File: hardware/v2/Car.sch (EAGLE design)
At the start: 63 parts

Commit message: Completed Rev.A of v2 hardware.
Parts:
- removed POW: (no value), SparkFun-Connectors:M02PTH4
- added J1: (no value), con-jack:DCJ0303
- renumbered 3.3V to 3V3, ARMS1 to M.ARMS, DIO1 to AIO, LED1 to HB, LED2 to PWR
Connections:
- net +12V: now also J1.2; no longer POW.1
- net GND: now also J1.1; no longer POW.2

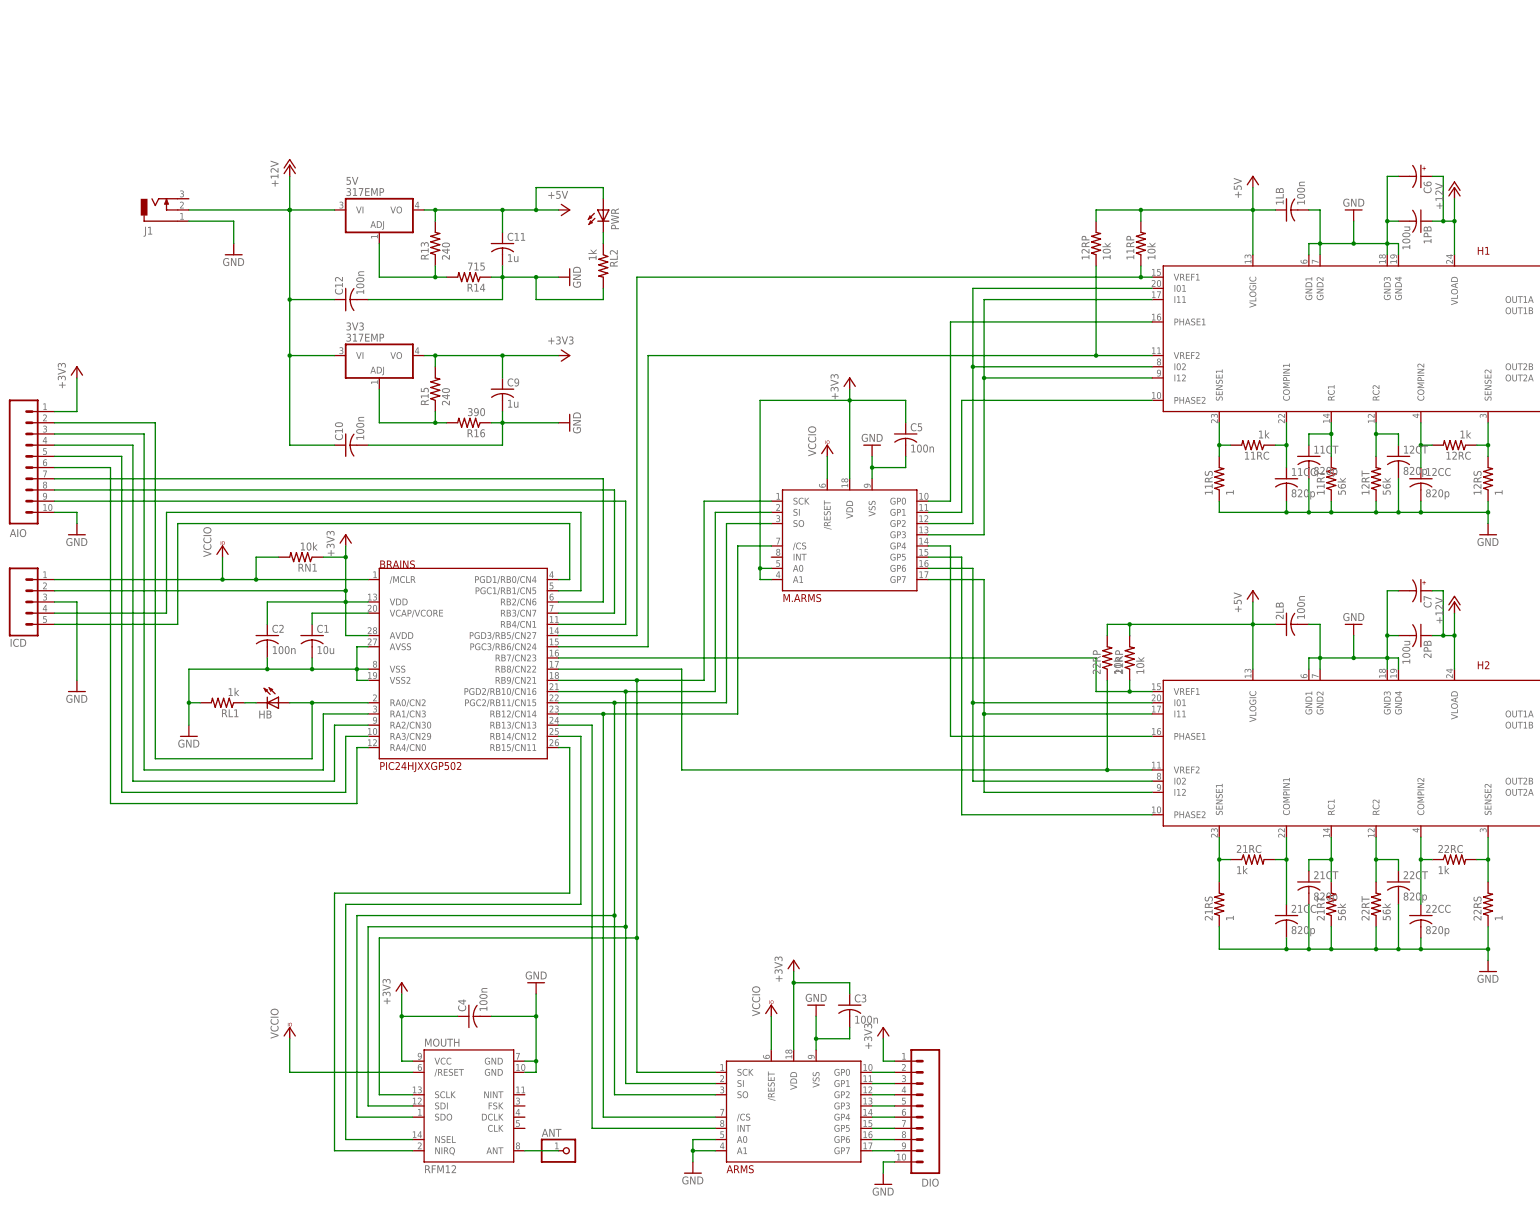
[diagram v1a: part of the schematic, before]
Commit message: Checkpointing. (about to make so potentially dangerous changes.)
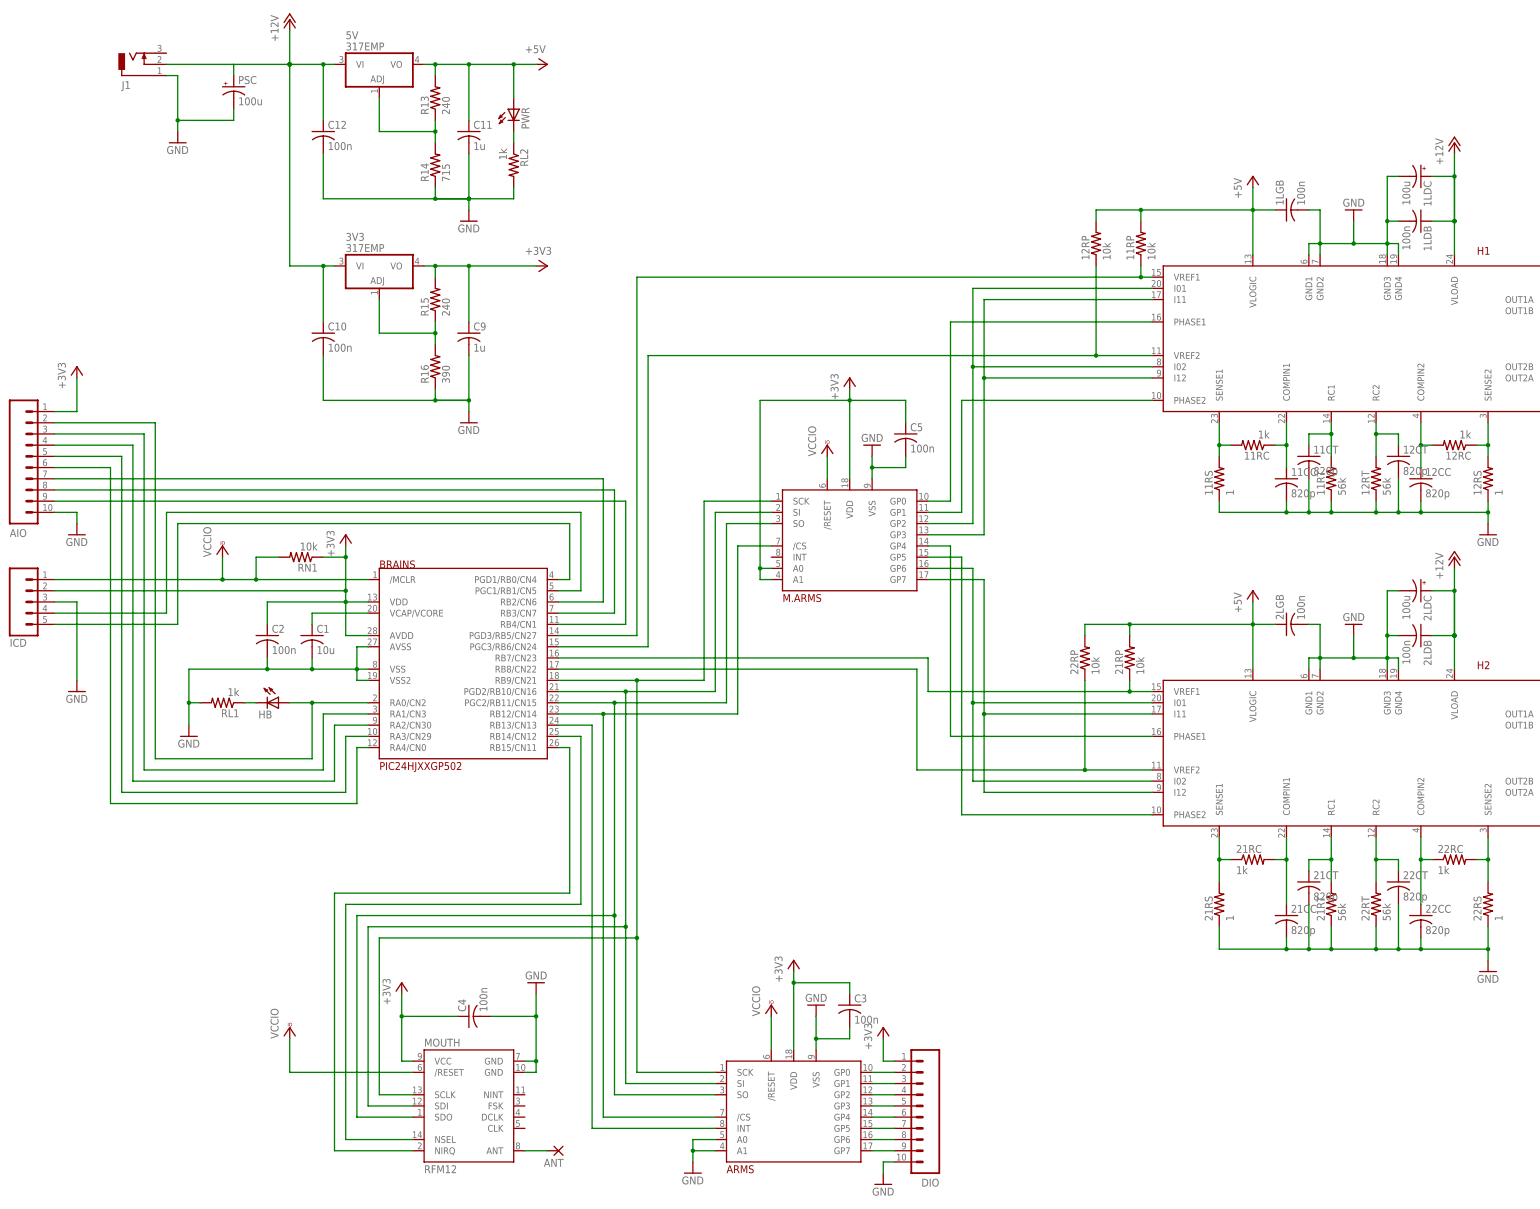
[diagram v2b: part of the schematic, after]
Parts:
- added PSC: 100u, SparkFun-Passives:CAP_POLC
- 1LDB, 2LDB: value 100u -> 100n
- 1LDC, 2LDC: value (none) -> 100u
- ANT: device pinhead:PINHD-1X1 -> wirepad:2,15/1,0
- renumbered 1LB to 1LGB, 1PB to 1LDB, 2LB to 2LGB, 2PB to 2LDB, C6 to 1LDC, C7 to 2LDC
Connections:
- removed net N$39: ANT.1, MOUTH.ANT
- new net N$11: ANT.P, MOUTH.ANT
- net +12V: now also PSC.+
- net GND: now also PSC.-
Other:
- moved on the sheet: 22RP, 3V3, 5V, C10, C11, C12, C9, J1, PWR, R13, R14, R15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

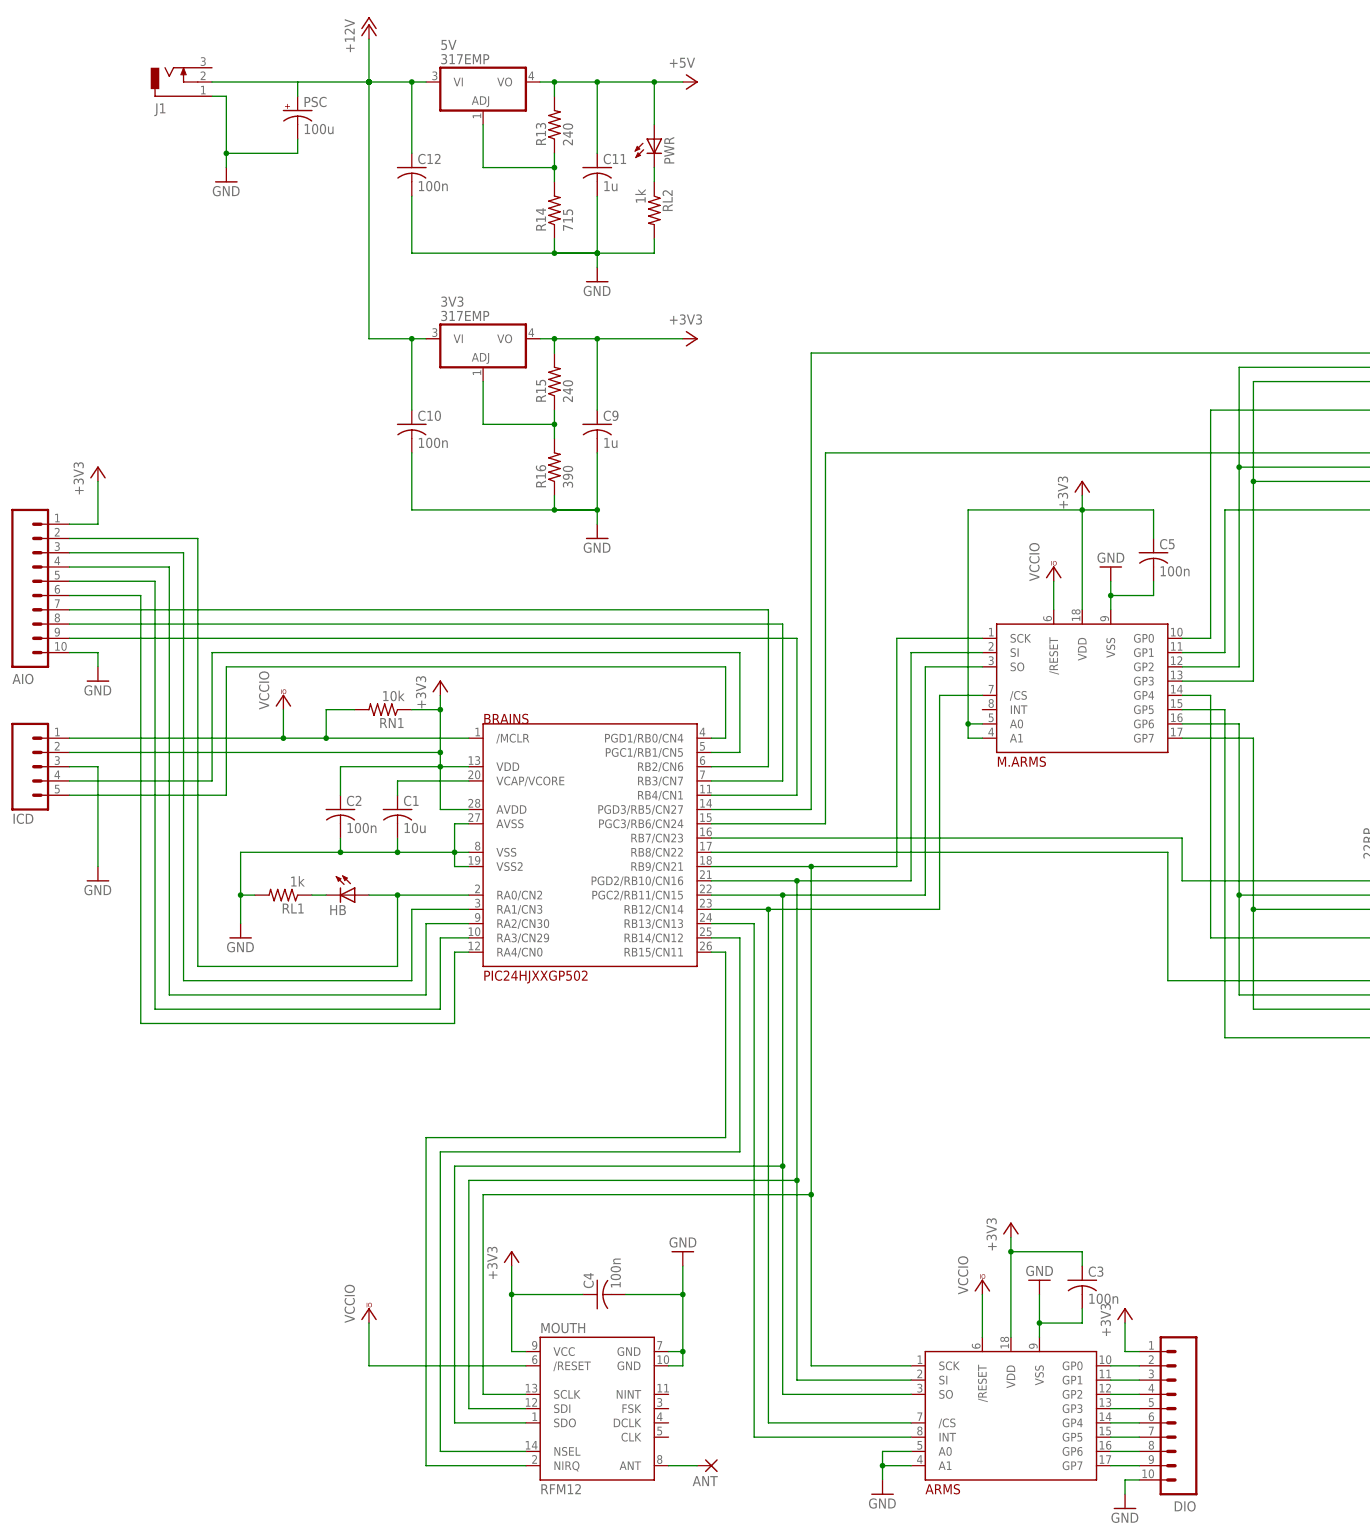
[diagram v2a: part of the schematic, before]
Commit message: Fixed a number of issues discovered from Rev. A boards.
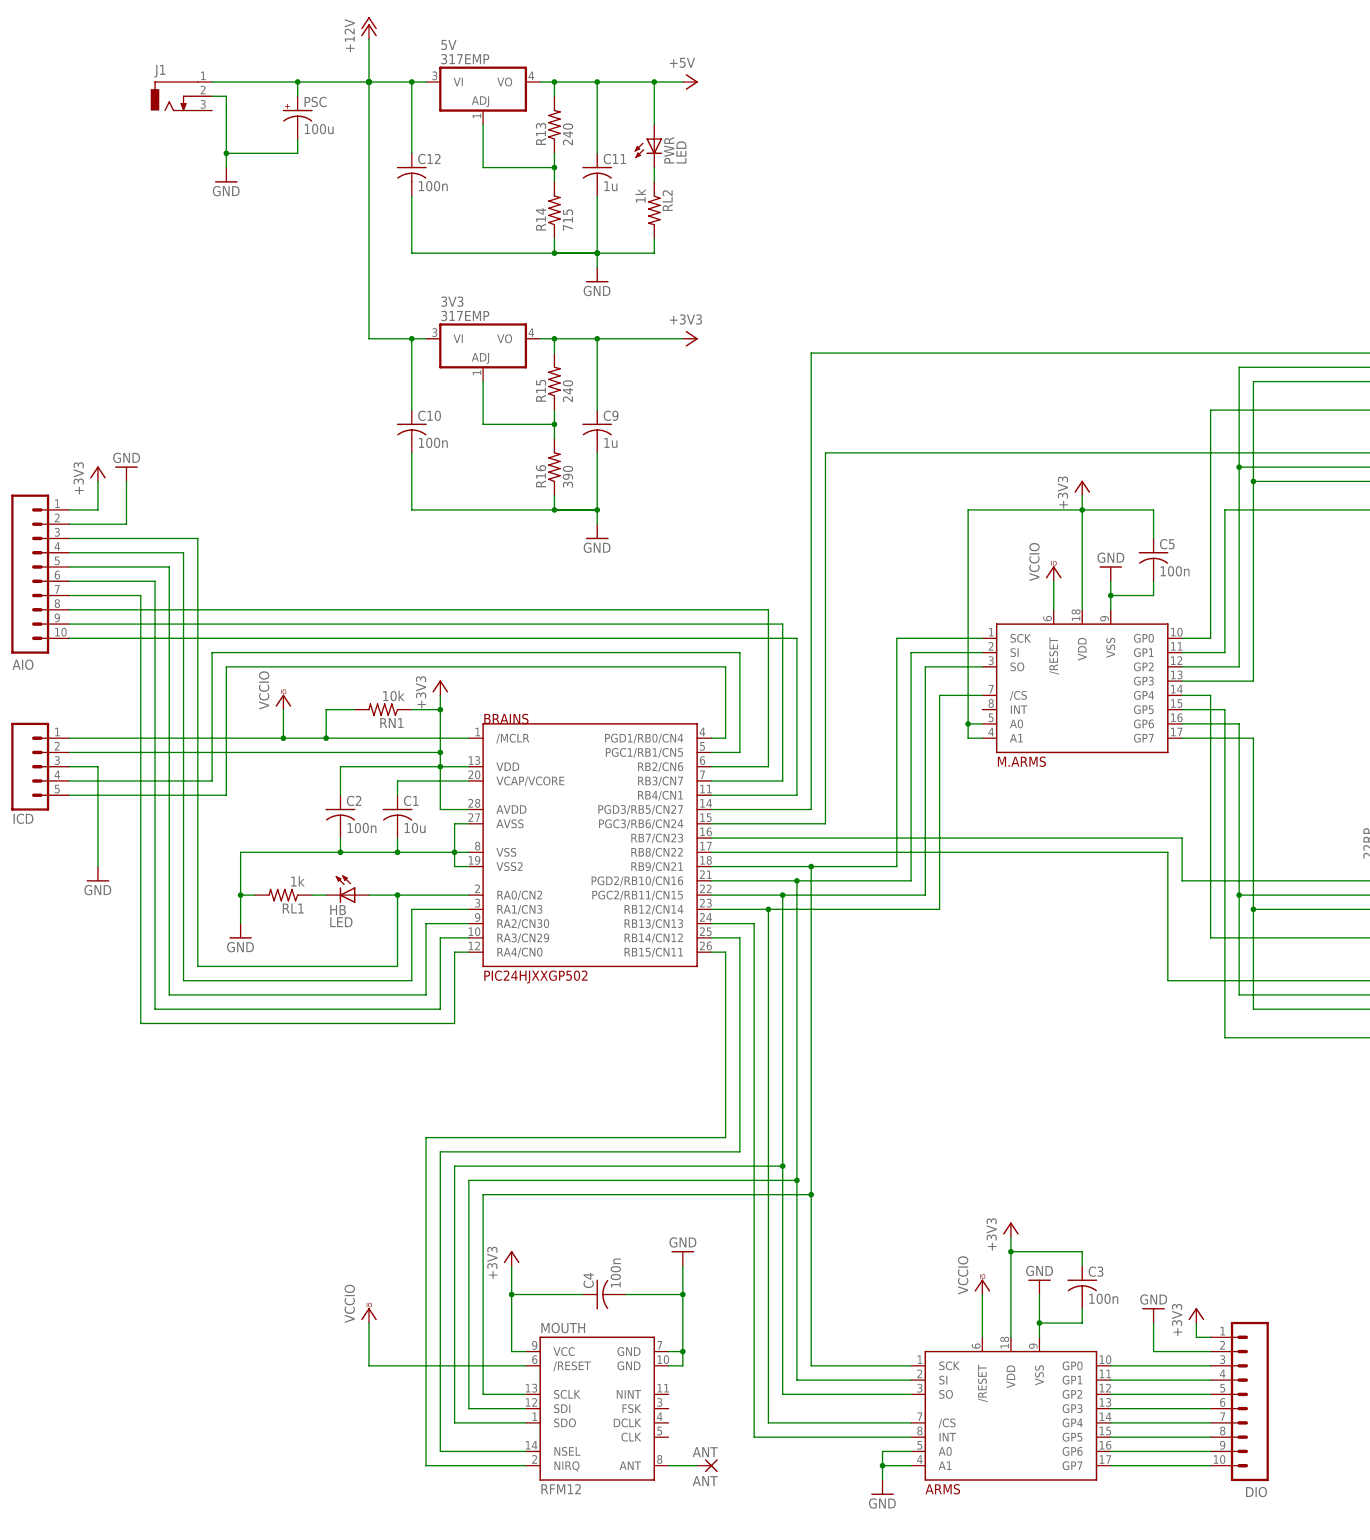
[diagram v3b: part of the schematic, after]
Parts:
- ANT: value (none) -> ANT
- HB, PWR: value (none) -> LED
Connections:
- removed net N$51: ARMS.GP5, DIO.7
- removed net N$52: ARMS.GP7, DIO.9
- new net N$39: ARMS.GP1, DIO.4
- new net N$47: ARMS.GP4, DIO.7
- net +12V: now also J1.1; no longer J1.2
- net GND: now also AIO.2, DIO.2, J1.2; no longer AIO.10, DIO.10, J1.1
- net N$12: now also ARMS.GP0, DIO.3; no longer ARMS.GP6, DIO.8
- net N$29: now also AIO.5; no longer AIO.4
- net N$32: now also AIO.6; no longer AIO.5
- net N$43: now also ARMS.GP2, DIO.5; no longer ARMS.GP0, DIO.2
- net N$44: now also ARMS.GP3, DIO.6; no longer ARMS.GP1, DIO.3
- net N$45: now also AIO.3; no longer AIO.2
- net N$48: now also ARMS.GP5, DIO.8; no longer ARMS.GP2, DIO.4
- net N$49: now also ARMS.GP6, DIO.9; no longer ARMS.GP3, DIO.5
- net N$50: now also ARMS.GP7, DIO.10; no longer ARMS.GP4, DIO.6
- net N$53: now also AIO.4; no longer AIO.3
- net N$54: now also AIO.8; no longer AIO.7
- net N$55: now also AIO.9; no longer AIO.8
- net N$57: now also AIO.7; no longer AIO.6
- net N$59: now also AIO.10; no longer AIO.9
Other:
- moved on the sheet: AIO, DIO, J1

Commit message: Minor cleanup.
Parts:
- removed C10, C12: 100n, rcl:C-USC0805
- removed PSC: 100u, SparkFun-Passives:CAP_POLC
- added PSB1: 100u, SparkFun-Passives:CAP_POLC
- added PSB2: 1u, rcl:C-USC0805
- added PSB3: 100n, rcl:C-USC0805
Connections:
- net +12V: now also PSB1.+, PSB2.1, PSB3.1; no longer C10.1, C12.1, PSC.+
- net GND: now also J1.3, PSB1.-, PSB2.2, PSB3.2; no longer C10.2, C12.2, J1.2, PSC.-
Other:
- moved on the sheet: J1

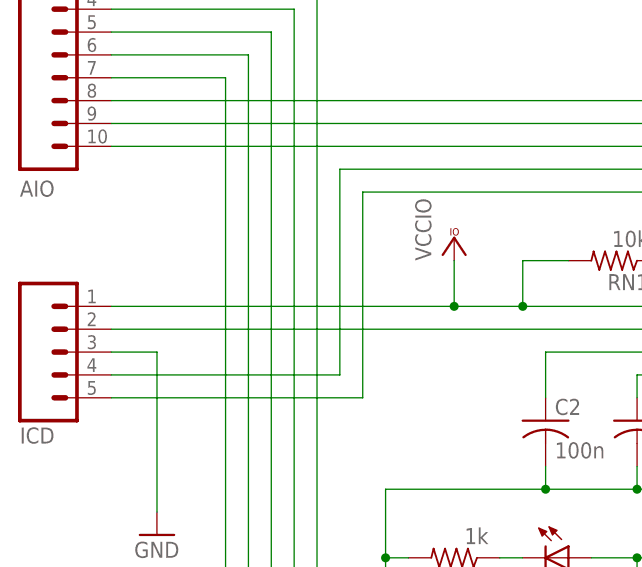
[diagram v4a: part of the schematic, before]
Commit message: Fixed PGD/PGC error (swapped) in schematic.
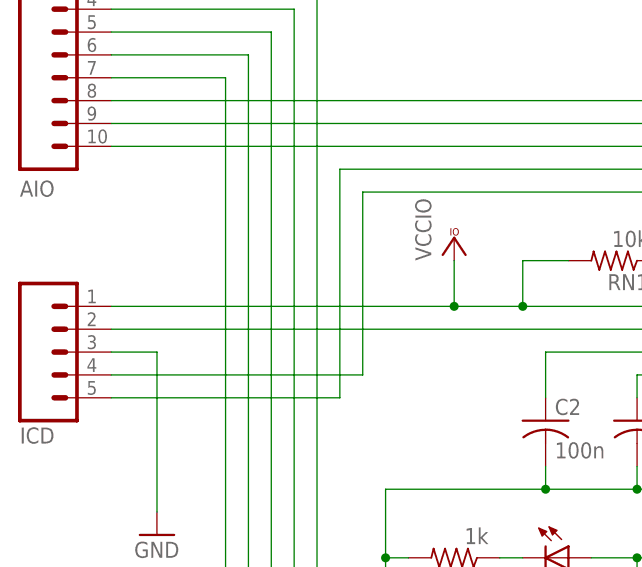
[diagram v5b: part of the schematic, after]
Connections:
- net N$28: now also ICD.5; no longer ICD.4
- net N$3: now also ICD.4; no longer ICD.5
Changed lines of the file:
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@@
 <?xml version="1.0" encoding="utf-8"?>
 <!DOCTYPE eagle SYSTEM "eagle.dtd">
-<eagle version="7.1.0">
+<eagle version="7.2.0">
 <drawing>
 <settings>
@@
 <wire x1="10.16" y1="63.5" x2="10.16" y2="76.2" width="0.1524" layer="91"/>
 <pinref part="BRAINS" gate="G$1" pin="PGD1/RB0/CN4"/>
-<wire x1="-78.74" y1="76.2" x2="-78.74" y2="53.34" width="0.1524" layer="91"/>
-<wire x1="-78.74" y1="53.34" x2="-106.68" y2="53.34" width="0.1524" layer="91"/>
-<pinref part="ICD" gate="G$1" pin="5"/>
+<pinref part="ICD" gate="G$1" pin="4"/>
+<wire x1="-106.68" y1="55.88" x2="-78.74" y2="55.88" width="0.1524" layer="91"/>
+<wire x1="-78.74" y1="55.88" x2="-78.74" y2="76.2" width="0.1524" layer="91"/>
 </segment>
 </net>
@@
 <wire x1="12.7" y1="78.74" x2="-81.28" y2="78.74" width="0.1524" layer="91"/>
 <pinref part="BRAINS" gate="G$1" pin="PGC1/RB1/CN5"/>
-<wire x1="-81.28" y1="78.74" x2="-81.28" y2="55.88" width="0.1524" layer="91"/>
-<wire x1="-81.28" y1="55.88" x2="-106.68" y2="55.88" width="0.1524" layer="91"/>
-<pinref part="ICD" gate="G$1" pin="4"/>
-</segment>
-</net>
+<wire x1="-81.28" y1="78.74" x2="-81.28" y2="53.34" width="0.1524" layer="91"/>
+<pinref part="ICD" gate="G$1" pin="5"/>
+<wire x1="-81.28" y1="53.34" x2="-106.68" y2="53.34" width="0.1524" layer="91"/>
+</segment>
+</net>
